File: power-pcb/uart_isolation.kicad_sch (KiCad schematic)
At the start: 9 parts, among them J11 Screw_Terminal_01x04, U21 ADUM1201AR, U22 SRV05-4

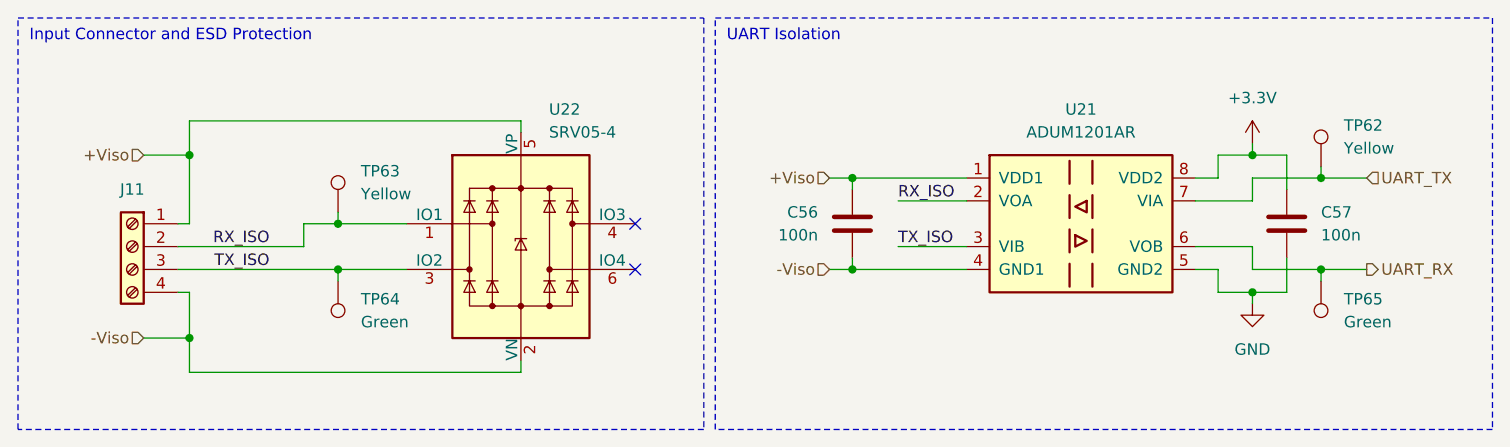
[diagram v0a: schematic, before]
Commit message: power-pcb: re-annotate schematic and start board
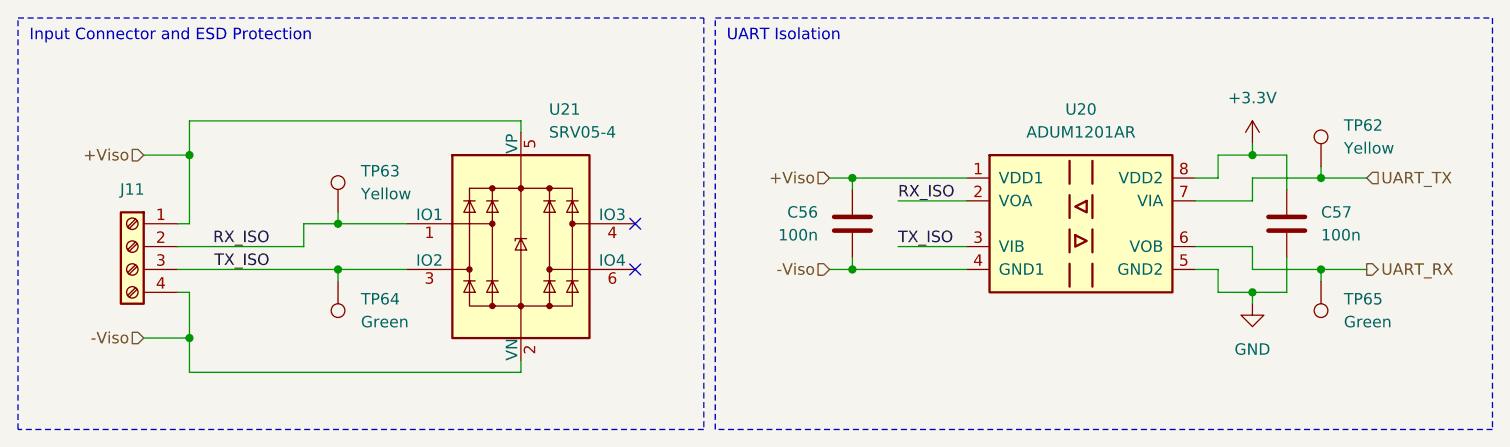
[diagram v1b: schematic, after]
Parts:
- renumbered U21 to U20, U22 to U21
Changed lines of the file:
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@@
 		(dnp no)
 		(fields_autoplaced yes)
-		(property "Reference" "U22"
+		(property "Reference" "U21"
 			(at 71.6981 22.86 0)
 			(show_name no)
@@
 			(project "power-pcb"
 				(path "/4b4cf3aa-c94c-4150-b9c5-35049cd71136/98c47c69-e753-45d5-a949-1f6e782e8c07/2d58b10e-b287-4680-9ee0-dcd6b4903146"
-					(reference "U24")
+					(reference "U23")
 					(unit 1)
 					(variant
@@
 				)
 				(path "/4b4cf3aa-c94c-4150-b9c5-35049cd71136/98c47c69-e753-45d5-a949-1f6e782e8c07/be987d2c-a213-4c25-b0fe-9b4345968d50"
-					(reference "U26")
+					(reference "U25")
 					(unit 1)
 					(variant
@@
 				)
 				(path "/4b4cf3aa-c94c-4150-b9c5-35049cd71136/98c47c69-e753-45d5-a949-1f6e782e8c07/d07c0ed4-3b58-4869-8743-63525d6d46a2"
-					(reference "U22")
+					(reference "U21")
 					(unit 1)
 					(variant
@@
 		(dnp no)
 		(fields_autoplaced yes)
-		(property "Reference" "U21"
+		(property "Reference" "U20"
 			(at 130.81 22.86 0)
 			(show_name no)
@@
 			(project "power-pcb"
 				(path "/4b4cf3aa-c94c-4150-b9c5-35049cd71136/98c47c69-e753-45d5-a949-1f6e782e8c07/2d58b10e-b287-4680-9ee0-dcd6b4903146"
-					(reference "U23")
+					(reference "U22")
 					(unit 1)
 					(variant
@@
 				)
 				(path "/4b4cf3aa-c94c-4150-b9c5-35049cd71136/98c47c69-e753-45d5-a949-1f6e782e8c07/be987d2c-a213-4c25-b0fe-9b4345968d50"
-					(reference "U25")
+					(reference "U24")
 					(unit 1)
 					(variant
@@
 				)
 				(path "/4b4cf3aa-c94c-4150-b9c5-35049cd71136/98c47c69-e753-45d5-a949-1f6e782e8c07/d07c0ed4-3b58-4869-8743-63525d6d46a2"
-					(reference "U21")
-					(unit 1)
-					(variant
+					(reference "U20")
+					(unit 1)
+					(variant

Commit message: power-pcb: fix schematic after review
- Add footprint for resitive load for the RECOM
- Add Opamps when useful
- Add capacitor and change some footprint sizes
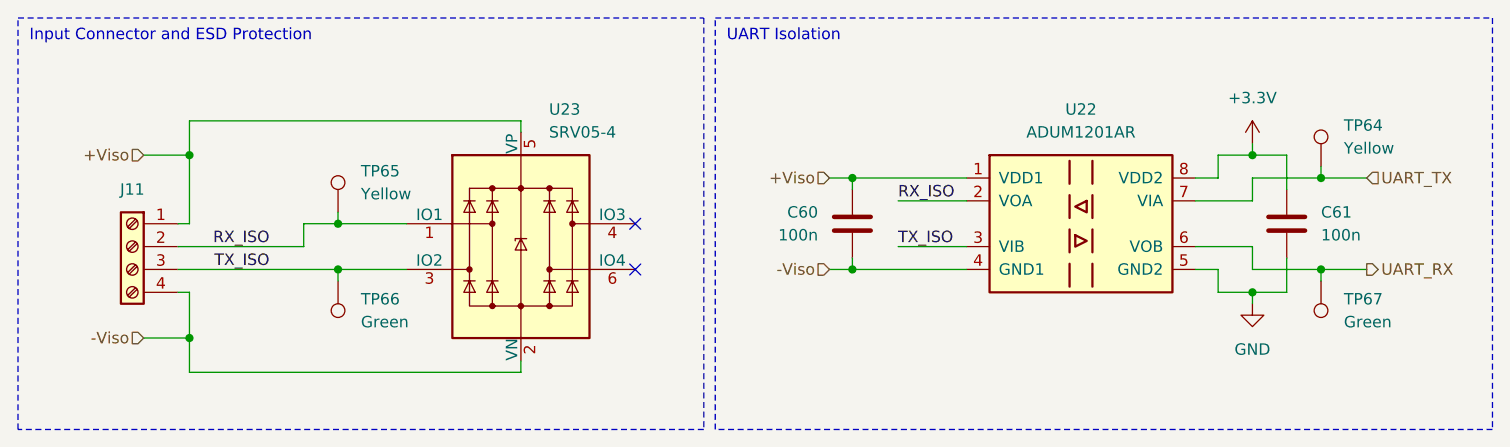
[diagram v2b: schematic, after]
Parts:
- C60: renamed from C56; footprint Capacitor_SMD:C_0603_1608Metric_Pad1.08x0.95mm_HandSolder -> Capacitor_SMD:C_0402_1005Metric_Pad0.74x0.62mm_HandSolder; JLCPCB C14663 -> C307331
- C61: renamed from C57; footprint Capacitor_SMD:C_0603_1608Metric_Pad1.08x0.95mm_HandSolder -> Capacitor_SMD:C_0402_1005Metric_Pad0.74x0.62mm_HandSolder; JLCPCB C14663 -> C307331
- renumbered TP62 to TP64, TP63 to TP65, TP64 to TP66, TP65 to TP67, U20 to U22, U21 to U23
